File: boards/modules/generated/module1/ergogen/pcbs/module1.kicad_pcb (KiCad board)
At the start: 2 copper layers, 75.2 x 75.2 mm, 19 parts

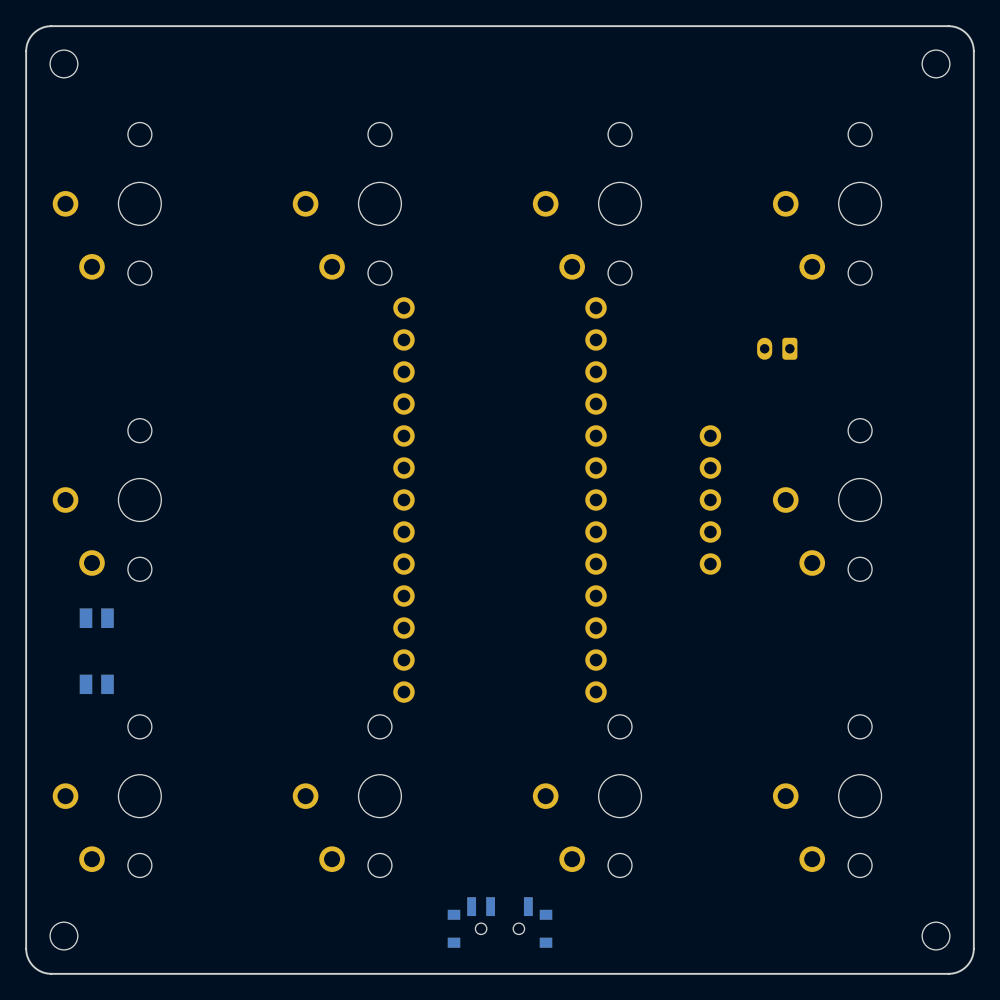
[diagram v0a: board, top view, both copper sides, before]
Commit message: Regenerate twelve-key module 1 PCB exports and underside-display previews
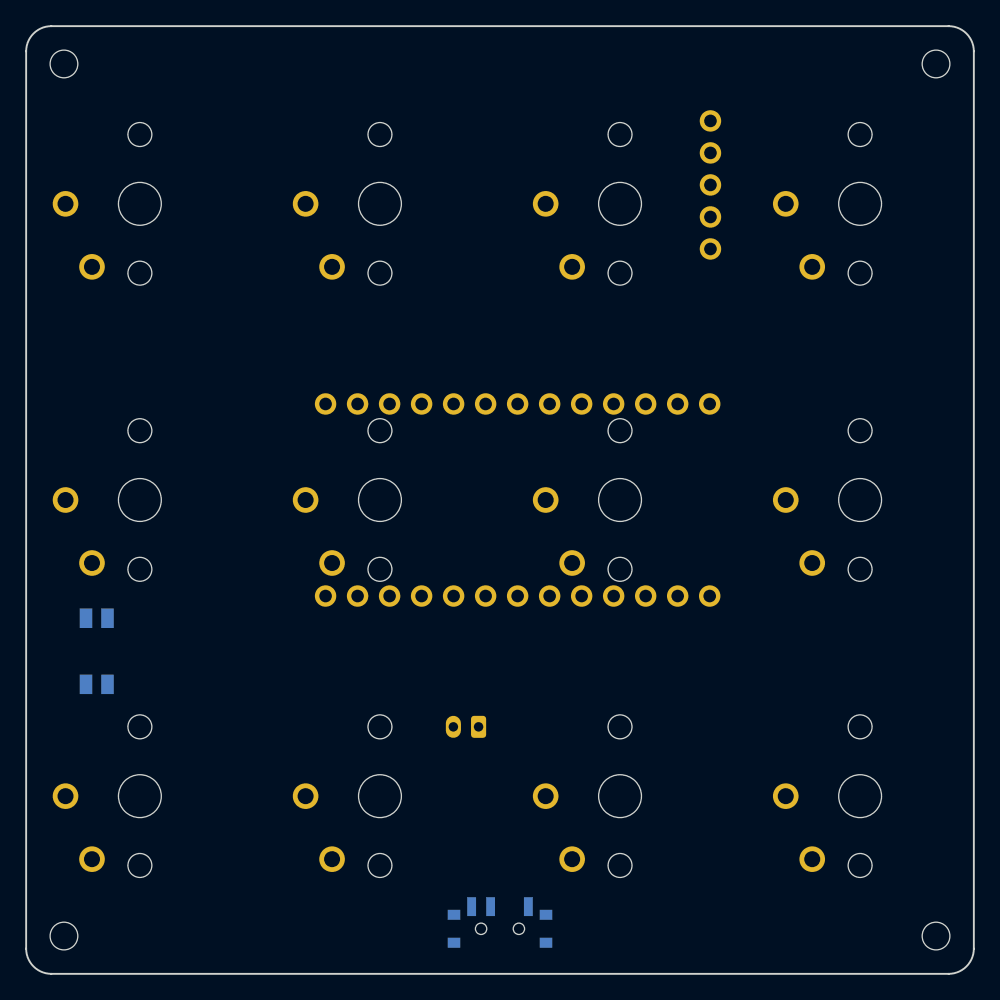
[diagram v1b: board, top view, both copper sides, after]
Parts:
- added S11: , switch_choc_v1_v2, F.Cu at (109.5, 123.5)
- added S12: , switch_choc_v1_v2, F.Cu at (128.6, 123.5)
- DISP1: moved to B.Cu
- moved S7 44.8 mm to (109.5, 100.0)
- moved S8 44.8 mm to (128.6, 100.0)
- moved JST1 38.9 mm to (97.3, 118.0)
- moved S9 38.1 mm to (71.4, 123.5)
- moved S10 38.1 mm to (90.5, 123.5)
- moved S6 38.1 mm to (90.5, 100.0)
- moved DISP1 25.0 mm to (100.0, 75.0)
- moved MCU1 1.40 mm to (101.4, 100.0), turned to 90 degrees
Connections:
- DISP1 pad 1: DISPLAY_MOSI -> DISPLAY_CS
- DISP1 pad 2: DISPLAY_SCK -> GND
- DISP1 pad 4: GND -> DISPLAY_SCK
- DISP1 pad 5: DISPLAY_CS -> DISPLAY_MOSI
- MCU1 pad 10: key_r3_c2 -> key_r2_c4
- MCU1 pad 11: key_r3_c4 -> key_r3_c2
- MCU1 pad 12: key_r3_c1 -> key_r2_c3
- MCU1 pad 13: key_r2_c4 -> key_r2_c2
- MCU1 pad 7: P19 -> key_r3_c4
- MCU1 pad 8: P18 -> key_r3_c3
- MCU1 pad 9: key_r3_c3 -> key_r3_c1
- S10 pad 2: key_r3_c4 -> key_r3_c2
- S6 pad 2: key_r2_c4 -> key_r2_c2
- S7 pad 2: key_r3_c1 -> key_r2_c3
- S8 pad 2: key_r3_c2 -> key_r2_c4
- S9 pad 2: key_r3_c3 -> key_r3_c1
